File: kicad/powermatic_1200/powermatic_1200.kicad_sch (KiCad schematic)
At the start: 33 parts, among them J1 T4171310004-001, J2 3PH-4W-PLUG, K1 HMC-9B30-11-DS, K2 HMC-9B30-11-DS, K3 HC3096N-52-900-24, K4 HMC-9B30-11-DS, K5 HMC-9B30-11-DS, K6 HMC-9B30-11-DS, M1 PWRM1200-MOTOR, Q1 FAZ-D4/2-NA-L, SW1 222102

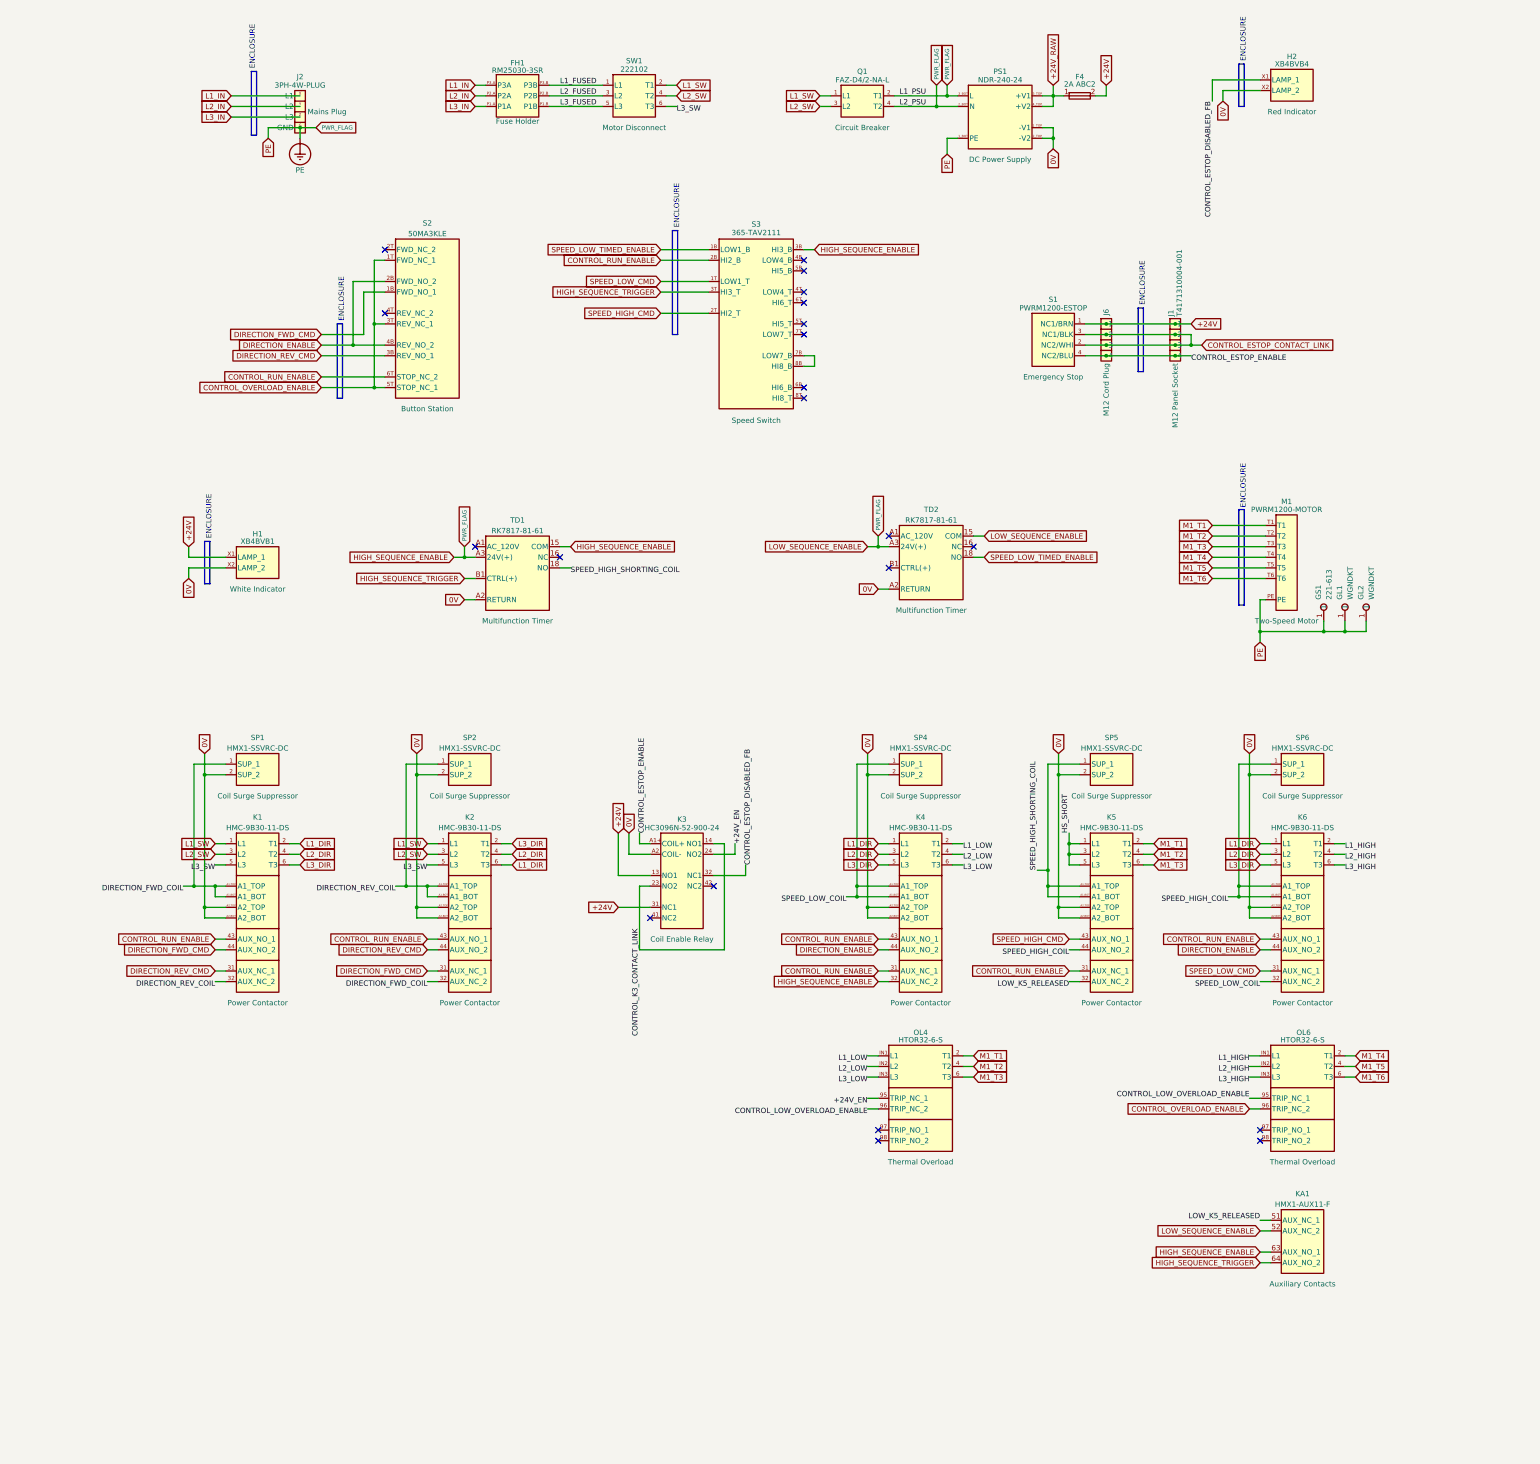
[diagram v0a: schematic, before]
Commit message: Update enclosure entries, terminal layout, and installation guides
Record right-face entry holes and relocate incoming power terminals while retaining their labels. Refresh wire lengths, BOM requirements, DIN layout, jumper guides, and saved schematic changes.

Specify two McMaster 9357K15 gasketed plugs for the unused motor/control entry pair and publish the Rev I portrait tabloid enclosure drawing.
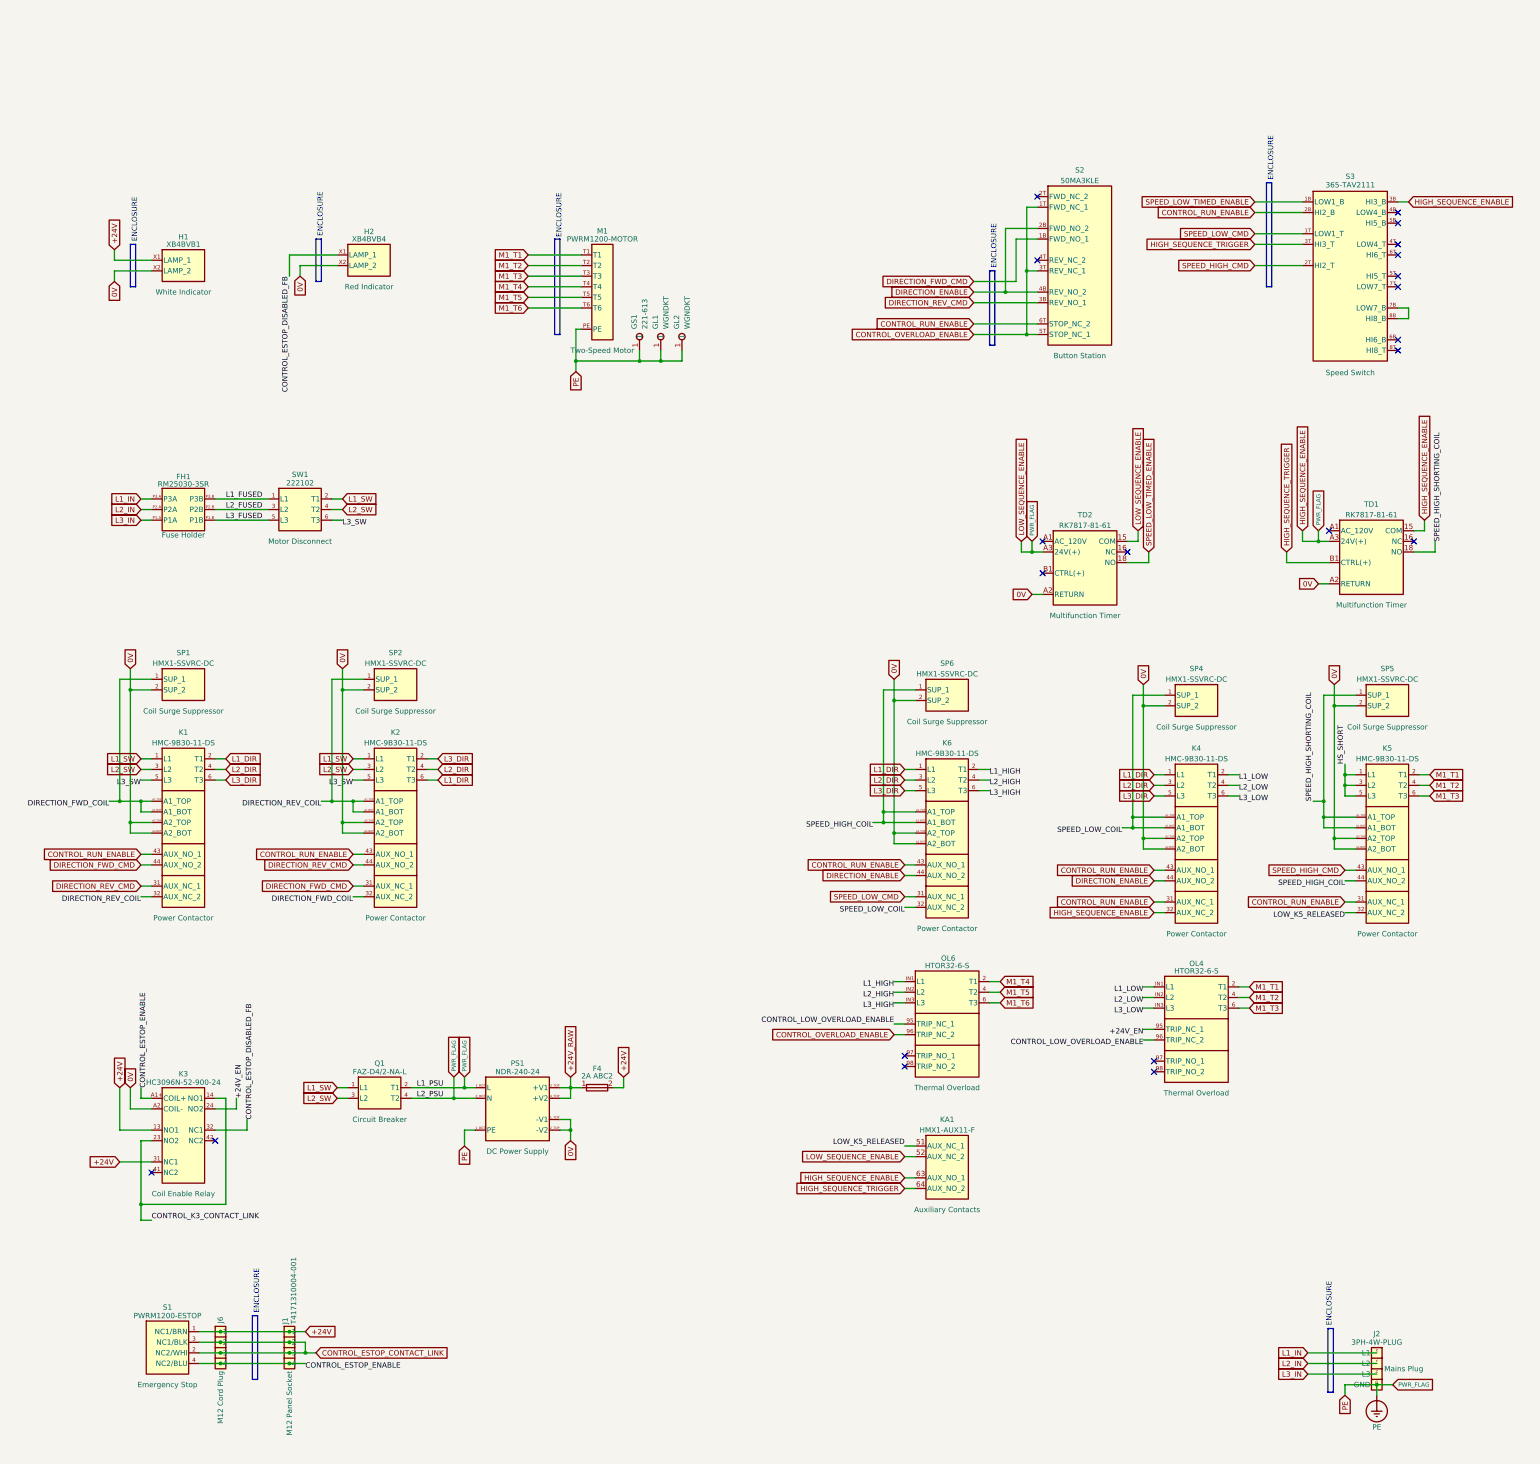
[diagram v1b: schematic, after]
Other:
- moved on the sheet: F4, FH1, GL1, GL2, GS1, H1, H2, J1, J2, J6, K1, K2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
